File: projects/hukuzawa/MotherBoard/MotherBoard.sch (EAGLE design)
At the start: 28 parts, among them IC1 PIC16F886, Q1 CERALOCK

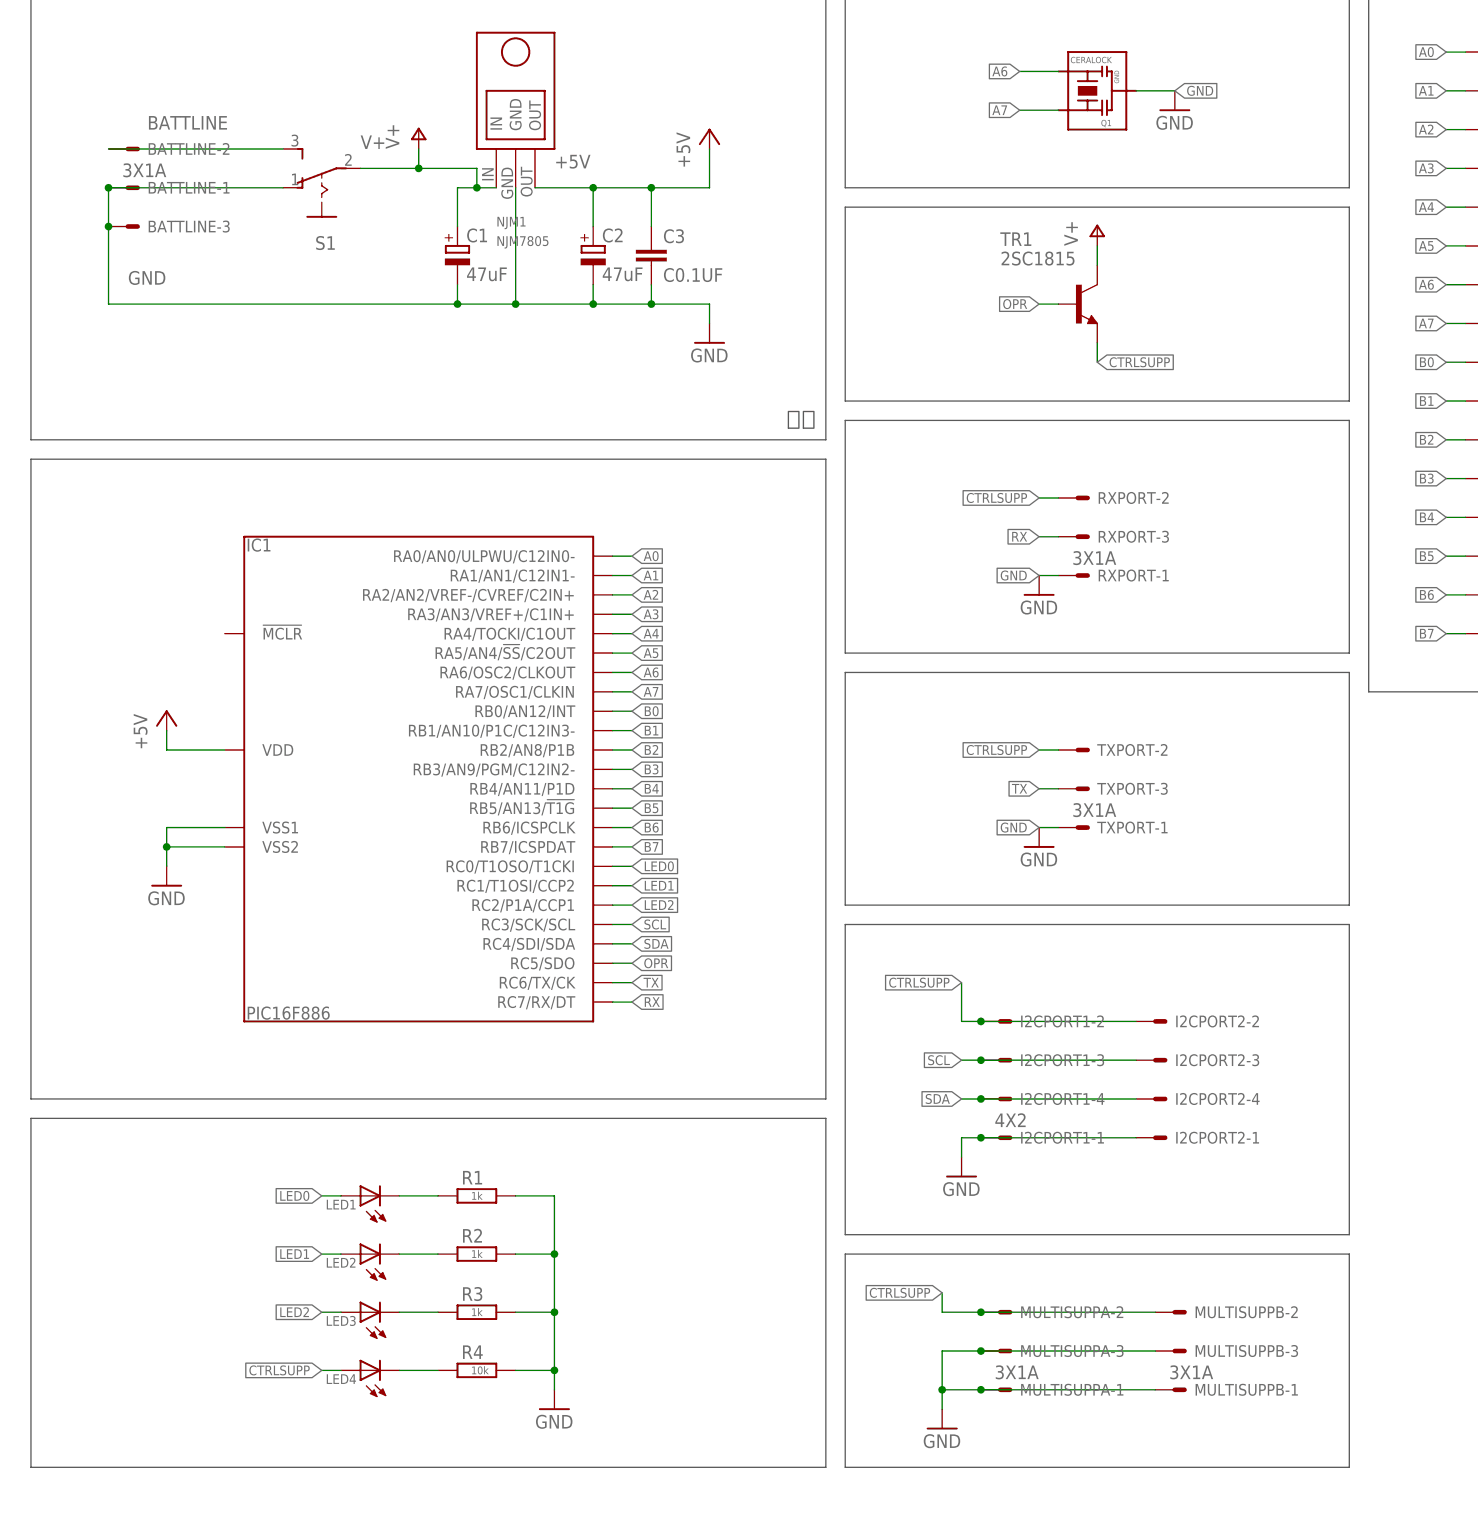
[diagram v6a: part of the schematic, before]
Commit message: マザーボード修正
規格化されたポートを分離、ライブラリを新規に作成
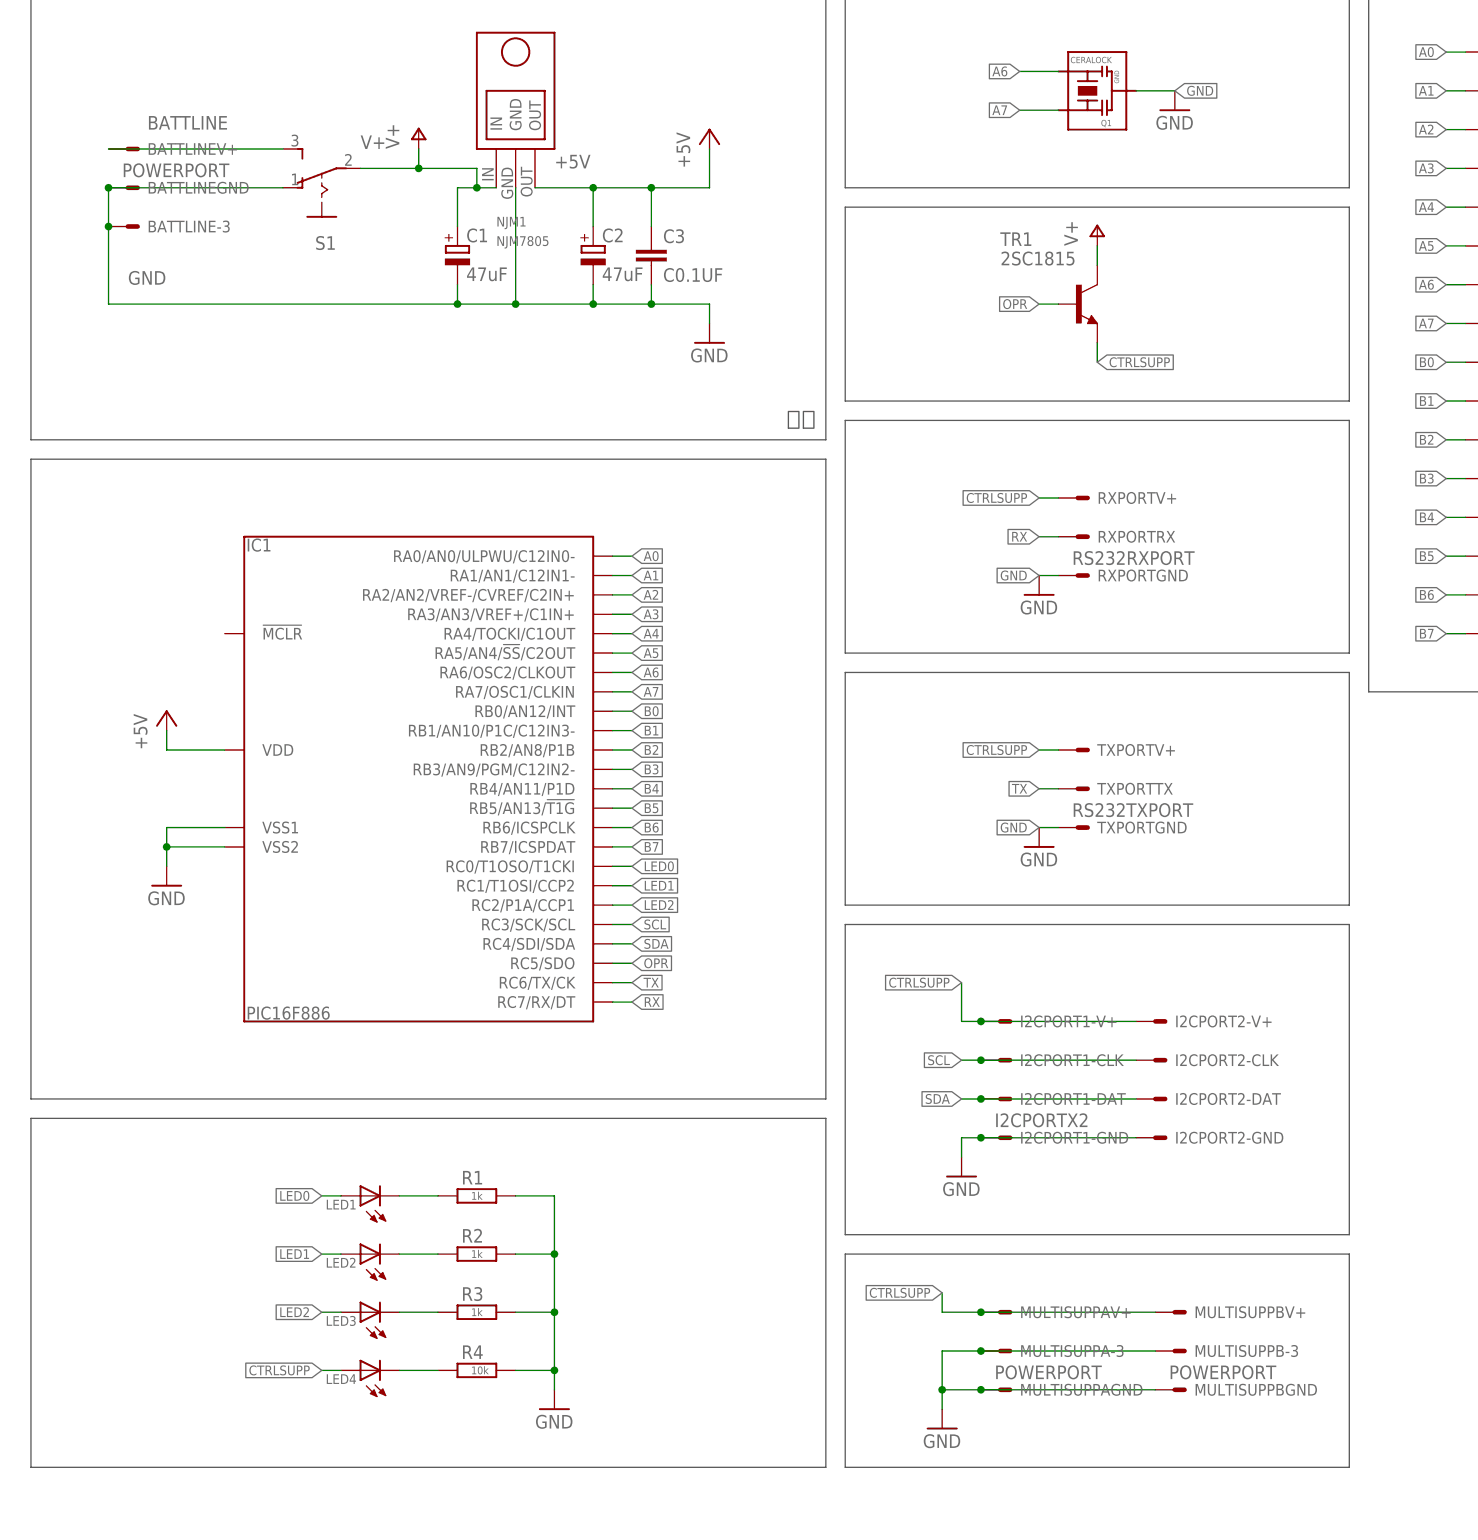
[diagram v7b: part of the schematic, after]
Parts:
- BATTLINE, MULTISUPPA, MULTISUPPB: value 3X1A -> POWERPORT; device 3M_372xx:3X1A -> 3M_Ports:POWERPORT
- I2CPORT: value 4X2 -> I2CPORTX2; device 3M_372xx:4X2 -> 3M_Ports:I2CPORTX2
- RXPORT: value 3X1A -> RS232RXPORT; device 3M_372xx:3X1A -> 3M_Ports:RS232RXPORT
- TXPORT: value 3X1A -> RS232TXPORT; device 3M_372xx:3X1A -> 3M_Ports:RS232TXPORT
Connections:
- net BATTLINE: now also BATTLINEV+.S; no longer BATTLINE-2.S
- net CTRLSUPP: now also I2CPORT1-V+.S, I2CPORT2-V+.S, MULTISUPPAV+.S, MULTISUPPBV+.S, RXPORTV+.S, TXPORTV+.S; no longer I2CPORT1-2.S, I2CPORT2-2.S, MULTISUPPA-2.S, MULTISUPPB-2.S, RXPORT-2.S, TXPORT-2.S
- net GND: now also BATTLINEGND.S, I2CPORT1-GND.S, I2CPORT2-GND.S, MULTISUPPAGND.S, MULTISUPPBGND.S, RXPORTGND.S, TXPORTGND.S; no longer BATTLINE-1.S, I2CPORT1-1.S, I2CPORT2-1.S, MULTISUPPA-1.S, MULTISUPPB-1.S, RXPORT-1.S, TXPORT-1.S
- net RX: now also RXPORTRX.S; no longer RXPORT-3.S
- net SCL: now also I2CPORT1-CLK.S, I2CPORT2-CLK.S; no longer I2CPORT1-3.S, I2CPORT2-3.S
- net SDA: now also I2CPORT1-DAT.S, I2CPORT2-DAT.S; no longer I2CPORT1-4.S, I2CPORT2-4.S
- net TX: now also TXPORTTX.S; no longer TXPORT-3.S
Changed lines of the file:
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@@
 </classes>
 <parts>
-<part name="BATTLINE" library="3M_372xx" deviceset="3X1" device="A"/>
+<part name="BATTLINE" library="3M_Ports" deviceset="POWERPORT" device=""/>
 <part name="NJM1" library="My_NJM7805" deviceset="NJM7805" device=""/>
 <part name="S1" library="switch" deviceset="SLIDESW" device=""/>
@@
 <part name="R4" library="rcl" deviceset="R-EU_" device="R3216W" value="10k"/>
 <part name="GND4" library="supply1" deviceset="GND" device=""/>
-<part name="TXPORT" library="3M_372xx" deviceset="3X1" device="A"/>
-<part name="RXPORT" library="3M_372xx" deviceset="3X1" device="A"/>
+<part name="TXPORT" library="3M_Ports" deviceset="RS232TXPORT" device=""/>
+<part name="RXPORT" library="3M_Ports" deviceset="RS232RXPORT" device=""/>
 <part name="GND7" library="supply1" deviceset="GND" device=""/>
 <part name="MULTIPORTA" library="3M_372xx" deviceset="4X2" device=""/>
 <part name="MULTIPORTB" library="3M_372xx" deviceset="4X2" device=""/>
-<part name="I2CPORT" library="3M_372xx" deviceset="4X2" device=""/>
+<part name="I2CPORT" library="3M_Ports" deviceset="I2CPORTX2" device=""/>
 <part name="Q1" library="FP-21T for MITS" deviceset="CERALOCK" device=""/>
 <part name="GND6" library="supply1" deviceset="GND" device=""/>
-<part name="MULTISUPPB" library="3M_372xx" deviceset="3X1" device="A"/>
-<part name="MULTISUPPA" library="3M_372xx" deviceset="3X1" device="A"/>
+<part name="MULTISUPPB" library="3M_Ports" deviceset="POWERPORT" device=""/>
+<part name="MULTISUPPA" library="3M_Ports" deviceset="POWERPORT" device=""/>
 <part name="GND8" library="supply1" deviceset="GND" device=""/>
 <part name="IC1" library="PIC" deviceset="PIC16F886" device=""/>
@@
 </plain>
 <instances>
-<instance part="BATTLINE" gate="-1" x="-180.34" y="93.98"/>
-<instance part="BATTLINE" gate="-2" x="-180.34" y="99.06"/>
+<instance part="BATTLINE" gate="GND" x="-180.34" y="93.98"/>
+<instance part="BATTLINE" gate="V+" x="-180.34" y="99.06"/>
 <instance part="BATTLINE" gate="-3" x="-180.34" y="88.9"/>
 <instance part="NJM1" gate="G$1" x="-132.08" y="104.14"/>
@@
 </instance>
 <instance part="GND4" gate="1" x="-127" y="-66.04"/>
-<instance part="TXPORT" gate="-1" x="-55.88" y="10.16"/>
-<instance part="TXPORT" gate="-2" x="-55.88" y="20.32"/>
-<instance part="TXPORT" gate="-3" x="-55.88" y="15.24"/>
-<instance part="RXPORT" gate="-1" x="-55.88" y="43.18"/>
-<instance part="RXPORT" gate="-2" x="-55.88" y="53.34"/>
-<instance part="RXPORT" gate="-3" x="-55.88" y="48.26"/>
+<instance part="TXPORT" gate="GND" x="-55.88" y="10.16"/>
+<instance part="TXPORT" gate="V+" x="-55.88" y="20.32"/>
+<instance part="TXPORT" gate="TX" x="-55.88" y="15.24"/>
+<instance part="RXPORT" gate="GND" x="-55.88" y="43.18"/>
+<instance part="RXPORT" gate="V+" x="-55.88" y="53.34"/>
+<instance part="RXPORT" gate="RX" x="-55.88" y="48.26"/>
 <instance part="GND7" gate="1" x="-63.5" y="40.64"/>
 <instance part="MULTIPORTA" gate="1-1" x="-2.54" y="111.76"/>
@@
 <instance part="MULTIPORTB" gate="2-3" x="-2.54" y="40.64"/>
 <instance part="MULTIPORTB" gate="2-4" x="-2.54" y="35.56"/>
-<instance part="I2CPORT" gate="1-1" x="-66.04" y="-30.48"/>
-<instance part="I2CPORT" gate="1-3" x="-66.04" y="-20.32"/>
-<instance part="I2CPORT" gate="1-2" x="-66.04" y="-15.24"/>
-<instance part="I2CPORT" gate="1-4" x="-66.04" y="-25.4"/>
-<instance part="I2CPORT" gate="2-1" x="-45.72" y="-30.48"/>
-<instance part="I2CPORT" gate="2-2" x="-45.72" y="-15.24"/>
-<instance part="I2CPORT" gate="2-3" x="-45.72" y="-20.32"/>
-<instance part="I2CPORT" gate="2-4" x="-45.72" y="-25.4"/>
+<instance part="I2CPORT" gate="1-GND" x="-66.04" y="-30.48"/>
+<instance part="I2CPORT" gate="1-CLK" x="-66.04" y="-20.32"/>
+<instance part="I2CPORT" gate="1-V+" x="-66.04" y="-15.24"/>
+<instance part="I2CPORT" gate="1-DAT" x="-66.04" y="-25.4"/>
+<instance part="I2CPORT" gate="2-GND" x="-45.72" y="-30.48"/>
+<instance part="I2CPORT" gate="2-V+" x="-45.72" y="-15.24"/>
+<instance part="I2CPORT" gate="2-CLK" x="-45.72" y="-20.32"/>
+<instance part="I2CPORT" gate="2-DAT" x="-45.72" y="-25.4"/>
 <instance part="Q1" gate="G$1" x="-55.88" y="106.68" rot="R90"/>
 <instance part="GND6" gate="1" x="-45.72" y="104.14"/>
-<instance part="MULTISUPPB" gate="-1" x="-43.18" y="-63.5"/>
-<instance part="MULTISUPPB" gate="-2" x="-43.18" y="-53.34"/>
+<instance part="MULTISUPPB" gate="GND" x="-43.18" y="-63.5"/>
+<instance part="MULTISUPPB" gate="V+" x="-43.18" y="-53.34"/>
 <instance part="MULTISUPPB" gate="-3" x="-43.18" y="-58.42"/>
-<instance part="MULTISUPPA" gate="-1" x="-66.04" y="-63.5"/>
-<instance part="MULTISUPPA" gate="-2" x="-66.04" y="-53.34"/>
+<instance part="MULTISUPPA" gate="GND" x="-66.04" y="-63.5"/>
+<instance part="MULTISUPPA" gate="V+" x="-66.04" y="-53.34"/>
 <instance part="MULTISUPPA" gate="-3" x="-66.04" y="-58.42"/>
 <instance part="GND8" gate="1" x="-76.2" y="-68.58"/>
@@
 </segment>
 <segment>
-<pinref part="I2CPORT" gate="1-3" pin="S"/>
-<pinref part="I2CPORT" gate="2-3" pin="S"/>
+<pinref part="I2CPORT" gate="1-CLK" pin="S"/>
+<pinref part="I2CPORT" gate="2-CLK" pin="S"/>
 <wire x1="-71.12" y1="-20.32" x2="-50.8" y2="-20.32" width="0.1524" layer="91"/>
 <wire x1="-71.12" y1="-20.32" x2="-73.66" y2="-20.32" width="0.1524" layer="91"/>
@@
 </segment>
 <segment>
-<pinref part="I2CPORT" gate="2-4" pin="S"/>
-<pinref part="I2CPORT" gate="1-4" pin="S"/>
+<pinref part="I2CPORT" gate="2-DAT" pin="S"/>
+<pinref part="I2CPORT" gate="1-DAT" pin="S"/>
 <wire x1="-50.8" y1="-25.4" x2="-71.12" y2="-25.4" width="0.1524" layer="91"/>
 <wire x1="-71.12" y1="-25.4" x2="-73.66" y2="-25.4" width="0.1524" layer="91"/>
@@
 <junction x="-114.3" y="78.74"/>
 <pinref part="GND1" gate="1" pin="GND"/>
-<pinref part="BATTLINE" gate="-1" pin="S"/>
+<pinref part="BATTLINE" gate="GND" pin="S"/>
 <pinref part="BATTLINE" gate="-3" pin="S"/>
 <wire x1="-185.42" y1="93.98" x2="-185.42" y2="88.9" width="0.1524" layer="91"/>
@@
 </segment>
 <segment>
-<pinref part="RXPORT" gate="-1" pin="S"/>
+<pinref part="RXPORT" gate="GND" pin="S"/>
 <pinref part="GND7" gate="1" pin="GND"/>
 <wire x1="-63.5" y1="43.18" x2="-60.96" y2="43.18" width="0.1524" layer="91"/>
@@
 </segment>
 <segment>
-<pinref part="TXPORT" gate="-1" pin="S"/>
+<pinref part="TXPORT" gate="GND" pin="S"/>
 <pinref part="GND9" gate="1" pin="GND"/>
 <wire x1="-63.5" y1="10.16" x2="-60.96" y2="10.16" width="0.1524" layer="91"/>
@@
 </segment>
 <segment>
-<pinref part="I2CPORT" gate="1-1" pin="S"/>
-<pinref part="I2CPORT" gate="2-1" pin="S"/>
+<pinref part="I2CPORT" gate="1-GND" pin="S"/>
+<pinref part="I2CPORT" gate="2-GND" pin="S"/>
 <wire x1="-71.12" y1="-30.48" x2="-50.8" y2="-30.48" width="0.1524" layer="91"/>
 <wire x1="-73.66" y1="-30.48" x2="-71.12" y2="-30.48" width="0.1524" layer="91"/>
@@
 <segment>
 <pinref part="GND8" gate="1" pin="GND"/>
-<pinref part="MULTISUPPA" gate="-1" pin="S"/>
+<pinref part="MULTISUPPA" gate="GND" pin="S"/>
 <wire x1="-76.2" y1="-66.04" x2="-76.2" y2="-63.5" width="0.1524" layer="91"/>
 <wire x1="-76.2" y1="-63.5" x2="-71.12" y2="-63.5" width="0.1524" layer="91"/>
-<pinref part="MULTISUPPB" gate="-1" pin="S"/>
+<pinref part="MULTISUPPB" gate="GND" pin="S"/>
 <wire x1="-71.12" y1="-63.5" x2="-48.26" y2="-63.5" width="0.1524" layer="91"/>
 <junction x="-71.12" y="-63.5"/>
@@
 </segment>
 <segment>
-<pinref part="TXPORT" gate="-3" pin="S"/>
+<pinref part="TXPORT" gate="TX" pin="S"/>
 <wire x1="-60.96" y1="15.24" x2="-63.5" y2="15.24" width="0.1524" layer="91"/>
 <label x="-63.5" y="15.24" size="1.27" layer="95" rot="R180" xref="yes"/>
@@
 </segment>
 <segment>
-<pinref part="RXPORT" gate="-3" pin="S"/>
+<pinref part="RXPORT" gate="RX" pin="S"/>
 <wire x1="-60.96" y1="48.26" x2="-63.5" y2="48.26" width="0.1524" layer="91"/>
 <label x="-63.5" y="48.26" size="1.27" layer="95" rot="R180" xref="yes"/>
@@
 <net name="BATTLINE" class="0">
 <segment>
-<pinref part="BATTLINE" gate="-2" pin="S"/>
+<pinref part="BATTLINE" gate="V+" pin="S"/>
 <pinref part="S1" gate="1" pin="3"/>
 <wire x1="-185.42" y1="99.06" x2="-162.56" y2="99.06" width="0.1524" layer="91"/>
@@
 </segment>
 <segment>
-<pinref part="RXPORT" gate="-2" pin="S"/>
+<pinref part="RXPORT" gate="V+" pin="S"/>
 <wire x1="-63.5" y1="53.34" x2="-60.96" y2="53.34" width="0.1524" layer="91"/>
 <label x="-63.5" y="53.34" size="1.27" layer="95" rot="R180" xref="yes"/>
 </segment>
 <segment>
-<pinref part="TXPORT" gate="-2" pin="S"/>
+<pinref part="TXPORT" gate="V+" pin="S"/>
 <wire x1="-63.5" y1="20.32" x2="-60.96" y2="20.32" width="0.1524" layer="91"/>
 <label x="-63.5" y="20.32" size="1.27" layer="95" rot="R180" xref="yes"/>
 </segment>
 <segment>
-<pinref part="I2CPORT" gate="1-2" pin="S"/>
+<pinref part="I2CPORT" gate="1-V+" pin="S"/>
 <wire x1="-73.66" y1="-10.16" x2="-73.66" y2="-15.24" width="0.1524" layer="91"/>
 <wire x1="-73.66" y1="-15.24" x2="-71.12" y2="-15.24" width="0.1524" layer="91"/>
-<pinref part="I2CPORT" gate="2-2" pin="S"/>
+<pinref part="I2CPORT" gate="2-V+" pin="S"/>
 <wire x1="-50.8" y1="-15.24" x2="-71.12" y2="-15.24" width="0.1524" layer="91"/>
 <junction x="-71.12" y="-15.24"/>
@@
 </segment>
 <segment>
-<pinref part="MULTISUPPA" gate="-2" pin="S"/>
+<pinref part="MULTISUPPA" gate="V+" pin="S"/>
 <wire x1="-76.2" y1="-50.8" x2="-76.2" y2="-53.34" width="0.1524" layer="91"/>
 <wire x1="-76.2" y1="-53.34" x2="-71.12" y2="-53.34" width="0.1524" layer="91"/>
-<pinref part="MULTISUPPB" gate="-2" pin="S"/>
+<pinref part="MULTISUPPB" gate="V+" pin="S"/>
 <wire x1="-48.26" y1="-53.34" x2="-71.12" y2="-53.34" width="0.1524" layer="91"/>
 <junction x="-71.12" y="-53.34"/>
